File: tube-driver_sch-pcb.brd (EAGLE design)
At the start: 100 x 100 mm, 135 parts, among them CN1 KS 54, CN10 NO FIT, CN2 MUSB-05-S-B-SM-A, CN3 KS 54, CN4 KS 54, CN5 KS 54, CN6 KS 54, CN7 KS 54, CN8 KS 54, CN9 KS 54, Q4 MMBT3904, Q5 MMBT3904, SW1 RA SM TACT, SW2 RA SM TACT, SW3 RA SM TACT, U1 STM32L052C8, U10 TPS61500, U11 3.3V BUCK, U12 SN65HVD75D, U2 TPS61500, U3 TPS61500, U5 ESP32, U6 USBLC6-2SC6, U7 FT231X, U8 TPS61500

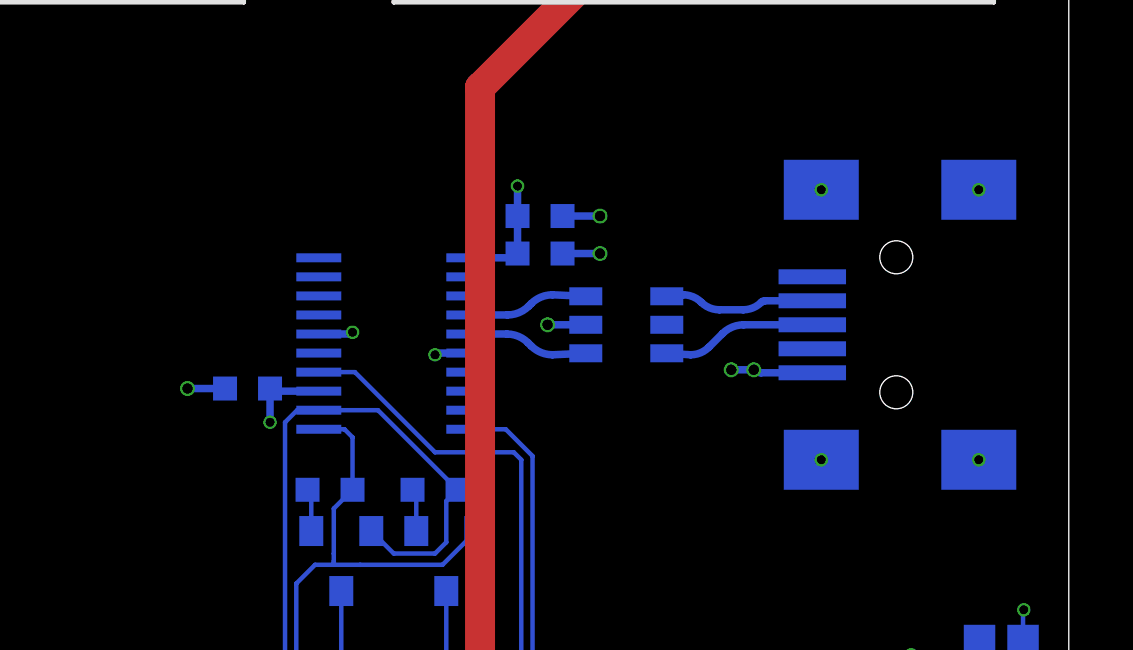
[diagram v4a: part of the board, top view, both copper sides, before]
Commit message: Improved BoM
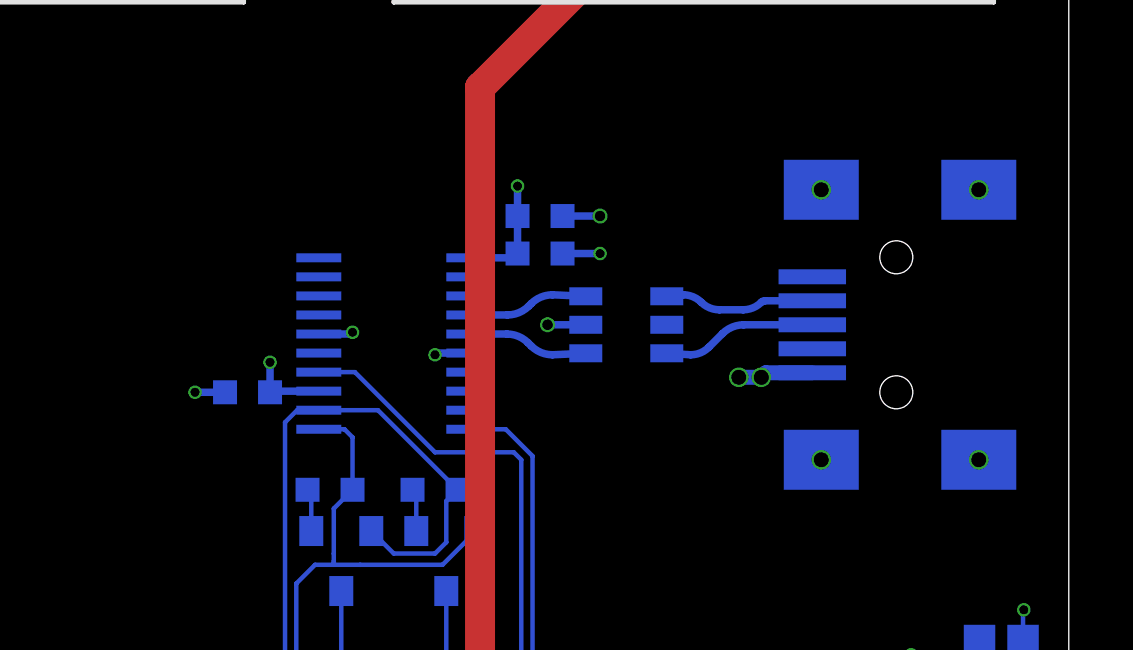
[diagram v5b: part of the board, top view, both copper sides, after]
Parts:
- C15, C17: value 100nF 50V -> 100nF 16V
- CN2: value MUSB-05-S-B-SM-A -> MINI B USB
- moved C17 10.8 mm to (72.6, 72.8), turned to 180 degrees
- moved C15 10.7 mm to (82.4, 77.4), turned to 0 degrees

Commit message: Working on rev 2
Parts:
- removed C15, C17, C33, C5, C6: 100nF 16V, CAPACITORS:0603
- removed C16: 2.2uF 25V, CAPACITORS:0603
- removed CN10: NO FIT, CONNECTORs:TSM-103-DV
- removed R18: 1.0k, r_0603:0603
- removed R32, R5: 10k, r_0603:0603
- removed R33: 120R, r_0603:0603
- removed SW2, SW3: RA SM TACT, ELECTROMECH:EVQP7*
- removed TP10, TP11, TP9: 2MM_TEST_POINT, MISC:2MM_TEST_PAD
- removed U12: SN65HVD75D, ICs:SO8
- removed U7: FT231X, ICs:SSOP20-4MM
- added D9: B360A-13-F, DIODES:DO214AC
- added FB1: 150R 100MHz, INDUCTORS:1206
- C2: value 100nF 16V -> 4.7uF 6.3V
- C4: value 100nF 16V -> 1nF 50V
- R2: value 10k -> 20k
- R4: value 1.0k -> 2.2k
- U1: value STM32L052C8 -> CP2102; device ICs:QFP48 -> ICs:QFN28
- moved C12 94.5 mm to (120.4, 125.2)
- moved R19 94.5 mm to (121.6, 125.2)
- moved R3 90.3 mm to (95.0, 39.4), turned to 0 degrees
- moved R4 88.8 mm to (95.0, 40.6), turned to 180 degrees
- moved R20 87.7 mm to (134.2, 123.8)
- moved C29 82.8 mm to (80.4, 7.62), turned to 0 degrees
- moved C30 80.0 mm to (80.4, 9.62), turned to 0 degrees
- moved U11 75.4 mm to (80.4, 13.0), turned to 270 degrees
- moved C31 70.2 mm to (80.4, 16.9), turned to 180 degrees
- moved C13 69.3 mm to (141.9, 83.1)
- moved C14 69.3 mm to (143.1, 83.1)
- moved R2 62.1 mm to (95.0, 41.9), turned to 0 degrees
- moved D6 59.7 mm to (79.5, 21.4), turned to 90 degrees
- moved C3 51.5 mm to (88.4, 27.5), turned to 90 degrees
- moved C7 51.0 mm to (77.2, 21.5)
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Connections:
- removed net ESP_INT: U1.14, U5.9
- removed net ESP_UART_RX: U1.12, U5.27
- removed net ESP_UART_TX: U1.13, U5.28
- removed net RS485_DE: R32.2, U1.33, U12.2, U12.3
- removed net RS485_UART_RX: U1.31, U12.1
- removed net RS485_UART_TX: U1.30, U12.4
- removed net RS485_USR_A: R33.2, TP9.1, U12.6
- removed net RS485_USR_B: R33.1, TP10.1, U12.7
- removed net STM_NRST: CN10.3, R2.1, U1.7
- removed net STM_SWCLK: CN10.4, U1.37
- removed net STM_SWDIO: CN10.5, U1.34
- removed net USER_BTN_0: C5.2, R4.1, U1.32
- removed net USER_BTN_1: C6.2, R18.1, U1.18
- new net 5VUSB: C3.2, C4.2, D9.A, FB1.2, R1.1, U6.5
- new net N$20: CN2.VCC, FB1.1
- new net N$7: C1.2, C2.2, U1.6, U1.7
- net 3V3: now also R4.2; no longer C1.2, C15.2, C16.2, C17.2, C2.2, C3.2, C33.2, C4.2, CN10.1, R2.2, R3.2, R5.2, U1.24, U1.36, U1.48, U1.9, U12.8, U7.13, U7.14, U7.15, U7.3
- net ESP32_UART_!DTR: now also U1.28; no longer U7.1
- net ESP32_UART_!RTS: now also U1.24; no longer U7.2
- net ESP32_UART_RX: now also U1.26; no longer U7.20
- net ESP32_UART_TX: now also U1.25; no longer U7.4
- net GND: now also R2.1, R3.1, U1.29, U1.3; no longer C15.1, C16.1, C17.1, C33.1, C5.1, C6.1, CN10.6, R1.1, R32.1, SW2.2, SW2.2', SW3.2, SW3.2', TP11.1, U1.23, U1.35, U1.47, U1.8, U12.5, U7.16, U7.6
- net LED_PWM_0: no longer U1.15
- net LED_PWM_1: no longer U1.11
- net LED_PWM_2: no longer U1.21
- net LED_PWM_3: no longer U1.22
- net N$1: now also R2.2, U1.8; no longer U1.44
- net N$2: now also R4.1, U1.9; no longer R3.1, R4.2, SW2.1, SW2.1'
- net N$3: now also R3.2, U1.11; no longer R18.2, R5.1, SW3.1, SW3.1'
- net N$97: now also U1.5; no longer U7.12
- net N$98: now also U1.4; no longer U7.11
- net VIN: now also D9.K
- net VOL_CONT: no longer U1.10
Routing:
- net LED_PWM_3: track 73.6 -> 5.31 mm, vias 2 -> 1
- net LED3_A: track 88.5 -> 24.0 mm, vias 2 -> 0
- net LED_PWM_0: track 61.9 -> 5.56 mm, vias 2 -> 1
- net LED1_A: track 86.4 -> 30.4 mm, vias 2 -> 0
- net LED2_A: track 86.4 -> 30.4 mm, vias 2 -> 0
- net LED0_A: track 86.4 -> 30.4 mm, vias 2 -> 0
- net USER_BTN_0: track 55.7 -> 0.00 mm
- net USER_BTN_1: track 45.2 -> 0.00 mm, vias 2 -> 0
- net ESP32_UART_!RTS: track 42.7 -> 0.00 mm
- net RS485_DE: track 41.9 -> 0.00 mm, vias 4 -> 0
- net RS485_UART_RX: track 41.9 -> 0.00 mm, vias 2 -> 0
- net LED_PWM_2: track 47.0 -> 5.56 mm, vias 2 -> 1
- net RS485_UART_TX: track 39.5 -> 0.00 mm, vias 2 -> 0
- net ESP_INT: track 38.8 -> 0.00 mm
- net GND: track 199.8 -> 164.7 mm, vias 171 -> 147
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
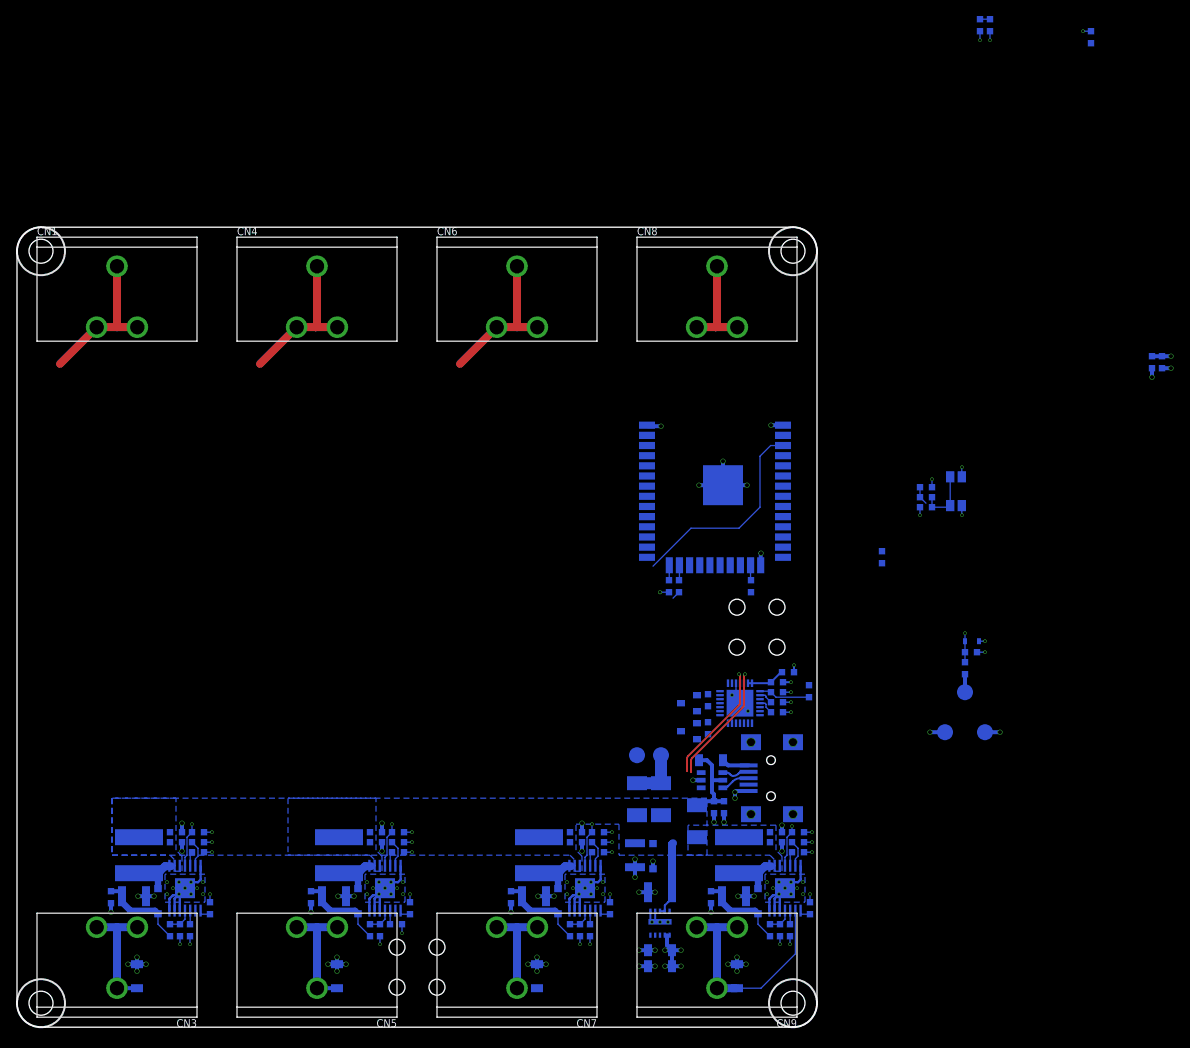
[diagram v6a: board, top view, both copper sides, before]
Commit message: Routed and passes DRC
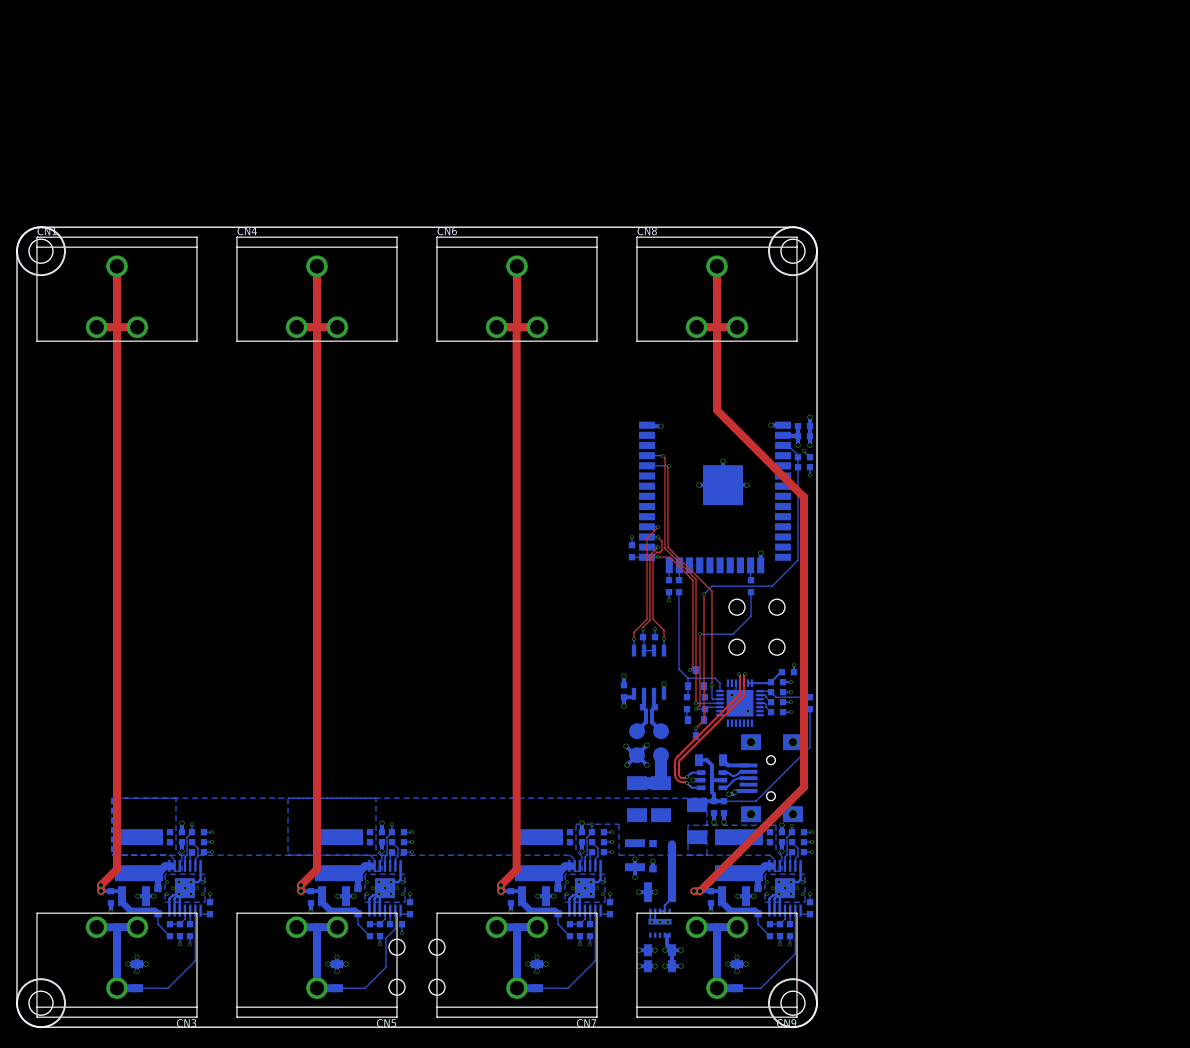
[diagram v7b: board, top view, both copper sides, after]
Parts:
- removed C20: 100nF 16V, CAPACITORS:0603
- removed C32: 1uF 25V, CAPACITORS:0603
- removed D8: PESD5Z3.3, DIODES:SC-79
- removed R11: 10k, r_0603:0603
- removed R16, R25: 1.0k, r_0603:0603
- removed R26: 100k, r_0603:0603
- removed SW1: RA SM TACT, ELECTROMECH:EVQP7*
- removed TP6, TP7, TP8: 2MM_TEST_POINT, MISC:2MM_TEST_PAD
- added C5: 100nF 16V, CAPACITORS:0603
- added R18: 120R, r_0603:0603
- added R5: 10k, r_0603:0603
- added TP3, TP4: 2MM_TEST_POINT, MISC:2MM_TEST_PAD
- added U4: SN65HVD75D, ICs:SO8
- moved R20 86.1 mm to (76.9, 59.5)
- moved C12 59.5 mm to (98.4, 70.0), turned to 0 degrees
- moved R19 58.8 mm to (98.4, 71.2), turned to 180 degrees
- moved C14 45.5 mm to (98.4, 75.1), turned to 0 degrees
- moved C13 44.5 mm to (98.4, 73.9), turned to 0 degrees
- moved Q5 6.68 mm to (84.9, 43.6), turned to 0 degrees
- moved Q4 3.25 mm to (84.9, 37.4), turned to 180 degrees
- moved R22 3.15 mm to (86.0, 40.5)
- moved R21 2.65 mm to (83.8, 40.5), turned to 90 degrees
- moved R1 1.51 mm to (99.1, 40.5), turned to 90 degrees
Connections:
- removed net N$4: R25.1, TP7.1
- removed net N$85: R11.1, R16.2, SW1.1, SW1.1'
- removed net VOL_CONT: C32.2, D8.K, R25.2, R26.2
- new net ESP_RS485_DE: R5.2, U4.2, U4.3, U5.26
- new net ESP_RS485_UART_RX: U4.4, U5.27
- new net ESP_RS485_UART_TX: U4.1, U5.28
- new net RS485_A: R18.2, TP3.1, U4.6
- new net RS485_B: R18.1, TP4.1, U4.7
- net 3V3: now also C5.2, U4.8; no longer R11.2, TP6.1
- net GND: now also C5.1, R5.1, U4.5; no longer C20.1, C32.1, D8.A, R26.1, SW1.2, SW1.2', TP8.1
- net USR_BTN_ESP: no longer C20.2, R16.1
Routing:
- net LED3_A: track 24.0 -> 107.3 mm, vias 0 -> 2
- net LED1_A: track 30.4 -> 99.7 mm, vias 0 -> 2
- net LED0_A: track 30.4 -> 99.8 mm, vias 0 -> 2
- net LED2_A: track 30.4 -> 99.7 mm, vias 0 -> 2
- net ESP32_UART_TX: track 0.00 -> 37.6 mm, vias 0 -> 2
- net ESP32_UART_RX: track 0.00 -> 35.2 mm, vias 0 -> 2
- net ESP32_UART_!RTS: track 0.00 -> 24.4 mm, vias 0 -> 2
- net ESP_IO0: track 0.01 -> 21.0 mm, vias 0 -> 2
- net ESP32_EN: track 27.5 -> 47.2 mm, vias 0 -> 2
- net ESP_RS485_UART_TX: track 0.00 -> 18.1 mm, vias 0 -> 2
- net 5VUSB: track 11.8 -> 29.7 mm
- net ESP32_UART_!DTR: track 1.06 -> 18.9 mm
- net LED2_K: track 12.7 -> 30.2 mm
- net LED0_K: track 15.2 -> 32.7 mm
- net LED1_K: track 15.5 -> 32.5 mm
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
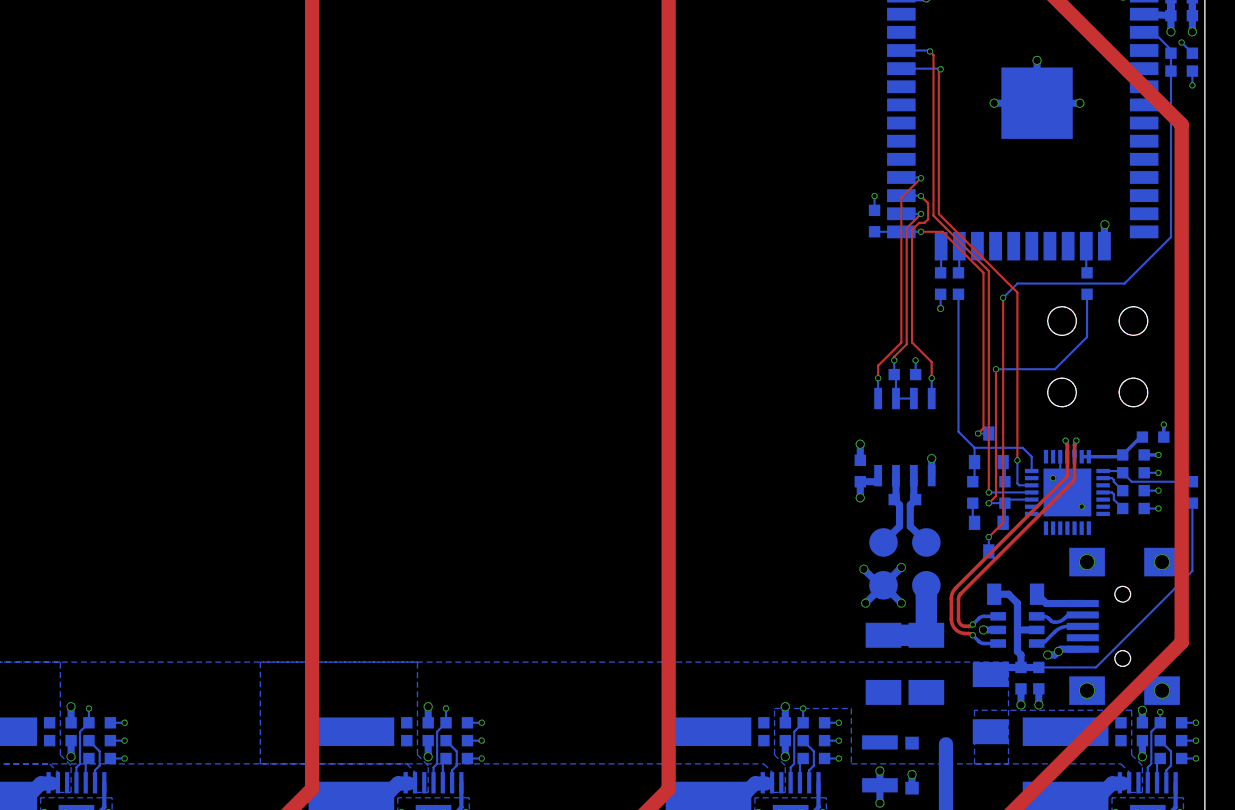
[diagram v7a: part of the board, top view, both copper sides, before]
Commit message: PWMs routed
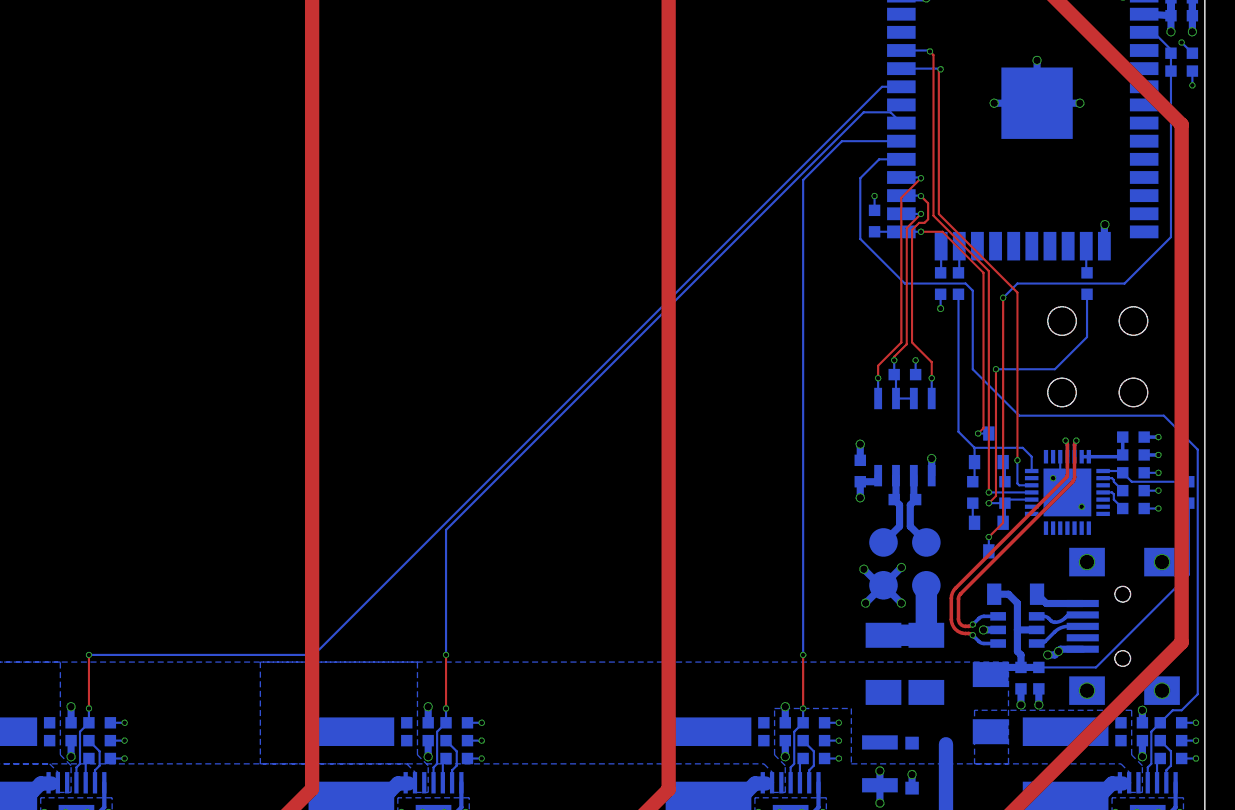
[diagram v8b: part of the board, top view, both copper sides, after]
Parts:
- moved C2 1.38 mm to (95.0, 44.4)
- moved R1 0.25 mm to (98.9, 40.5)
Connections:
- removed net USR_BTN_ESP: U5.29
- net LED_PWM_0: now also R41.2, U10.4, U5.29; no longer R10.2, U2.4
- net LED_PWM_1: now also R31.2, U5.30, U8.4; no longer R17.2, U3.4
- net LED_PWM_2: now also R17.2, U3.4, U5.31; no longer R31.2, U8.4
- net LED_PWM_3: now also R10.2, U2.4, U5.33; no longer R41.2, U10.4
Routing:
- net LED_PWM_3: track 5.31 -> 82.7 mm, vias 1 -> 2
- net LED_PWM_0: track 5.56 -> 65.8 mm, vias 1 -> 0
- net LED_PWM_2: track 5.56 -> 62.4 mm, vias 1 -> 2
- net LED_PWM_1: track 5.56 -> 50.6 mm, vias 1 -> 2
- net N$7: track 4.82 -> 4.18 mm
